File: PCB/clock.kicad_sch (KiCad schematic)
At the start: 104 parts, among them J1 PWR, J2 PWR, J3 EXT_TEMP, J4 EXT_TEMP, J5 PROG, Q1 BSS138, Q2 BSS138, Q3 BSS138, SW1 ENTER, SW2 PLUS, SW3 MINUS, SW4 ESC, U1 D148K, U10 DS9503P1, U11 D148K, U12 D148K, U13 D148K, U14 D148K, U15 D148K, U16 D148K, U17 D148K, U18 D148K, U19 MAX7219, U2 D148K, U20 DS3231MZ, U21 DS3231M, U22 D148K, U23 D148K, U24 D148K, U25 D148K, U26 D148K, U27 D148K, U28 MAX7219, U29 STM32F030F4Px, U3 D148K, U4 D148K, U5 D148K, U6 D148K, U7 LM1117DT-3.3, U8 MAX7219, U9 DS2482, Y1 10MHz

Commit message: PCB updated with final component values
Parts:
- D6: value MRA4007 -> SS16 SHOTTKY
- R1, R2, R3, R4: value 100 -> 0
- R13, R18: value 10k -> 47k
- R20, R21: value 3k3 -> 2k2
- R5: value 10k -> 13k7
- Y1: value 10MHz -> 8MHz
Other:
- note added: "Bridge SB1 by default"
- moved on the sheet: J4, R20, R21

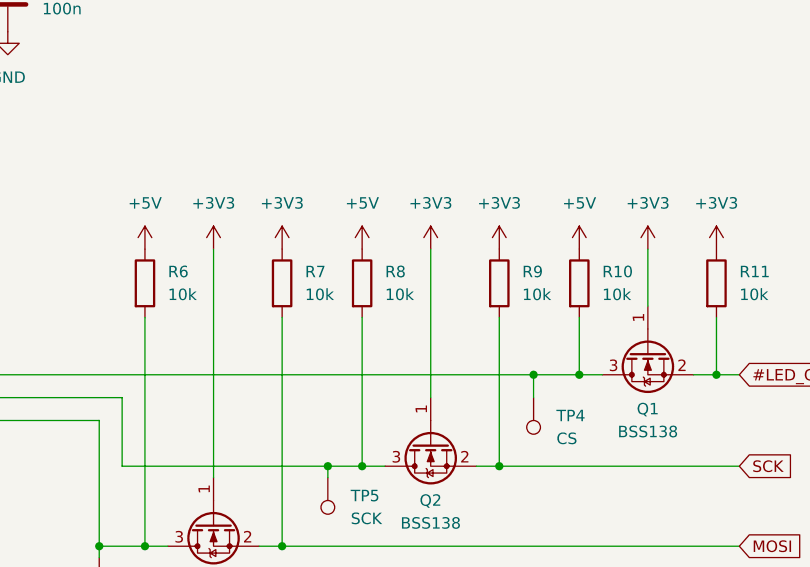
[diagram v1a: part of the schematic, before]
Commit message: Logic shifter resistors readjustment
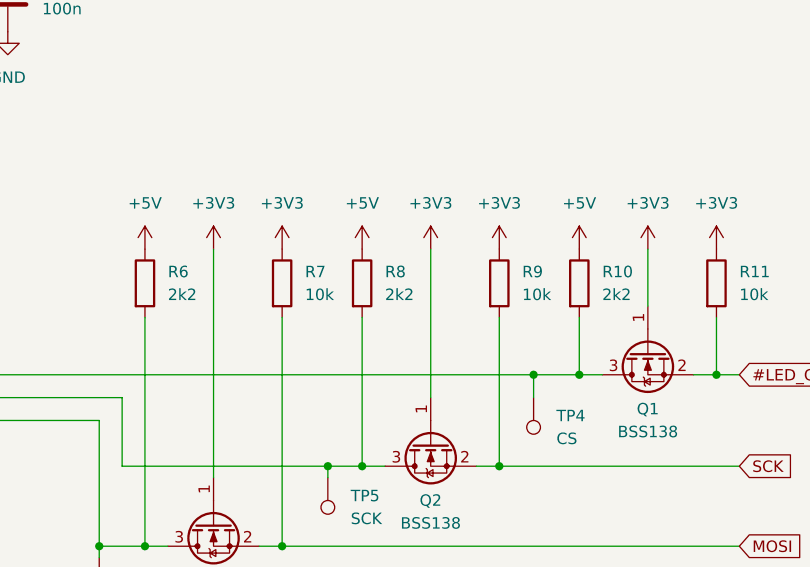
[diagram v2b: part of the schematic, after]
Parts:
- R10, R6, R8: value 10k -> 2k2
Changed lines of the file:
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@@
 		(fields_autoplaced yes)
 		(property "Reference" "R10"
-			(at 384.81 82.55 0)
+			(at 384.81 82.5499 0)
 			(effects
 				(font
@@
 			)
 		)
-		(property "Value" "10k"
-			(at 384.81 85.09 0)
+		(property "Value" "2k2"
+			(at 384.81 85.0899 0)
 			(effects
 				(font
@@
 		(fields_autoplaced yes)
 		(property "Reference" "R6"
-			(at 336.55 82.55 0)
+			(at 336.55 82.5499 0)
 			(effects
 				(font
@@
 			)
 		)
-		(property "Value" "10k"
-			(at 336.55 85.09 0)
+		(property "Value" "2k2"
+			(at 336.55 85.0899 0)
 			(effects
 				(font
@@
 		(fields_autoplaced yes)
 		(property "Reference" "R8"
-			(at 360.68 82.55 0)
+			(at 360.68 82.5499 0)
 			(effects
 				(font
@@
 			)
 		)
-		(property "Value" "10k"
-			(at 360.68 85.09 0)
+		(property "Value" "2k2"
+			(at 360.68 85.0899 0)
 			(effects
 				(font
